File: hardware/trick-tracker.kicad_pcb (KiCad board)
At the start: 4 copper layers, 31 x 45 mm, 53 parts, among them IC1 BMX160, J1 USB4105-GF-A, J2 S2B-PH-K, J3 QWiiC, J4 MEM2061-01-188-00-A, J6 QWiiC, P1 SMTB-1240-S-R, U1 MS88SF2, U2 DPS368XTSA1, U4 MCP73831/OT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

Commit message: Add Gerbers
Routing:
- net GND: vias 41 -> 44

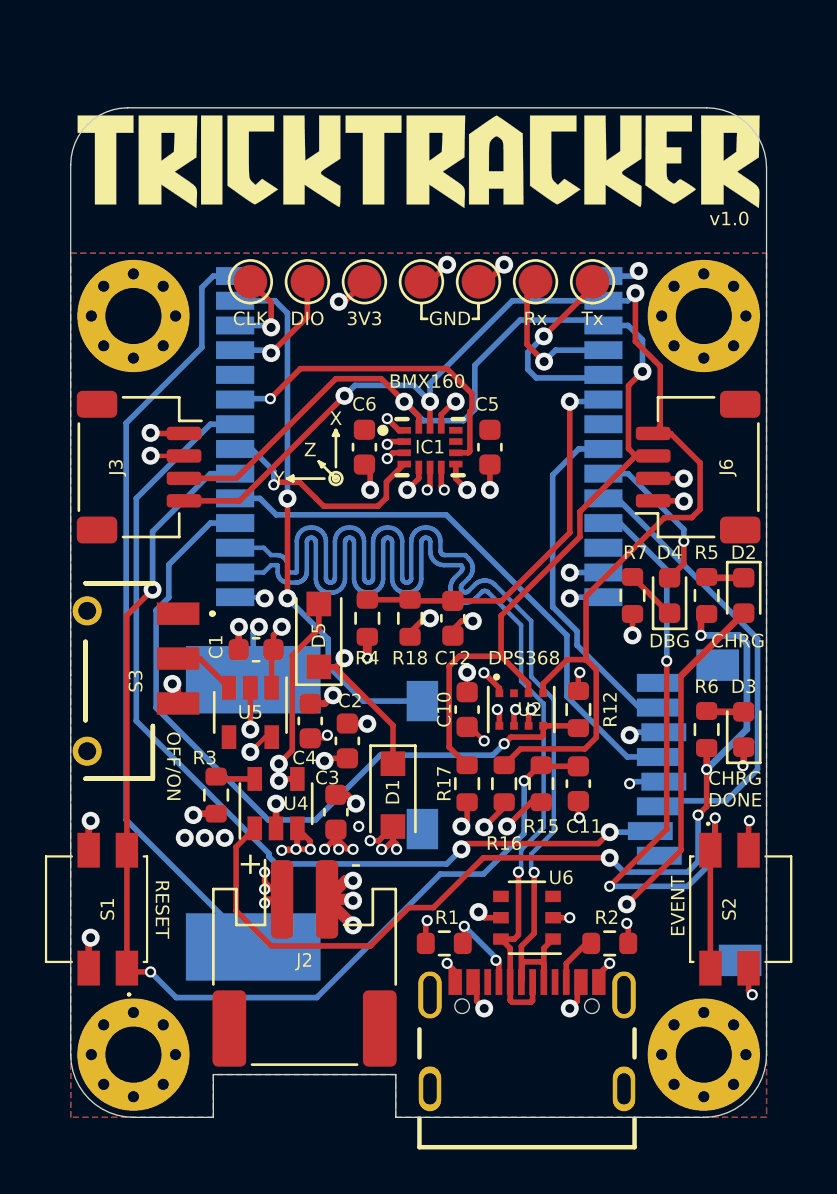
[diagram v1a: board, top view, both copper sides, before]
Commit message: Changed Layout to use ESP32 instead of nRF52
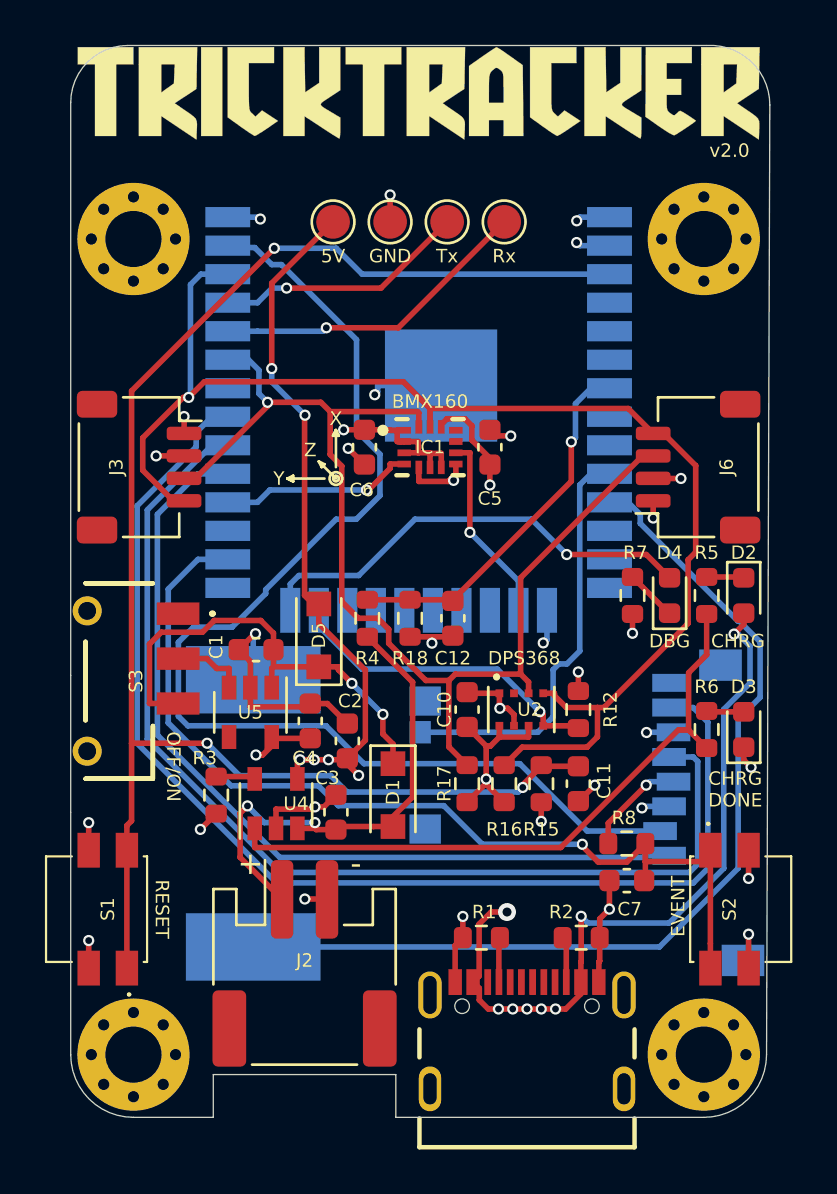
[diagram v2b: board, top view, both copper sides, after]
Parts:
- removed TP5: TP_3v3, TestPoint:TestPoint_Pad_D1.5mm
- removed TP6, TP7: TP_GND, TestPoint:TestPoint_Pad_D1.5mm
- removed U1: MS88SF2, MS88SF2:MS88SF2
- removed U6: IP4220CZ6, Package_SO:TSOP-6_1.65x3.05mm_P0.95mm
- added C7: 0.1µF, Capacitor_SMD:C_0603_1608Metric, F.Cu at (154.8, 126.5)
- added R8: 10k, Resistor_SMD:R_0603_1608Metric, F.Cu at (154.8, 124.8)
- added U3: ESP32-WROOM-32, RF_Module:ESP32-WROOM-32, B.Cu at (145.5, 105.2)
- J4: footprint MEM2061-01-188-00-A_REVA:GCT_MEM2061-01-188-00-A_REVA -> MEM2051-00-195-00-A:GCT_MEM2051-00-195-00-A
- TP1: value TP_Tx -> TestPoint
- TP2: value TP_Rx -> TestPoint
- TP3: value TP_SWDCLK -> TestPoint
- TP4: value TP_SWD -> TestPoint
- moved TP1 11.9 mm to (141.7, 97.2)
- moved TP3 9.16 mm to (146.8, 97.2)
- moved TP4 9.16 mm to (149.4, 97.2)
- moved TP2 7.00 mm to (144.3, 97.2)
- moved H3 3.43 mm to (132.8, 97.9)
- moved H4 3.43 mm to (158.2, 97.9)
- moved G*** 3.05 mm to (145.5, 91.4)
- moved R1 1.67 mm to (148.3, 129.0)
- moved R2 1.30 mm to (152.8, 129.0)
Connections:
- net /3.3V renamed +3V3
- IC1 pad 10: Net-(IC1-Pad10) -> unconnected-(IC1-Pad10)
- IC1 pad 11: Net-(IC1-Pad11) -> unconnected-(IC1-Pad11)
- J1 pad A6: /D+ -> unconnected-(J1-PadA6)
- J1 pad A7: /D- -> unconnected-(J1-PadA7)
- J1 pad A8: Net-(J1-PadA8) -> unconnected-(J1-PadA8)
- J1 pad B6: /D+ -> unconnected-(J1-PadB6)
- J1 pad B7: /D- -> unconnected-(J1-PadB7)
- J1 pad B8: Net-(J1-PadB8) -> unconnected-(J1-PadB8)
- J1 pad S1: Net-(J1-PadS1) -> unconnected-(J1-PadS1)
- J1 pad S2: Net-(J1-PadS2) -> unconnected-(J1-PadS2)
- J1 pad S3: Net-(J1-PadS3) -> unconnected-(J1-PadS3)
- J1 pad S4: Net-(J1-PadS4) -> unconnected-(J1-PadS4)
- J4 pad 1: Net-(J4-Pad1) -> /CS
- J4 pad 2: /CS -> /MOSI
- J4 pad 3: /MOSI -> GND
- J4 pad 5: /SCK -> /CLK
- J4 pad 8: Net-(J4-Pad8) -> unconnected-(J4-Pad8)
- S3 pad 1: Net-(S3-Pad1) -> unconnected-(S3-Pad1)
- S3 pad MH1: Net-(S3-PadMH1) -> unconnected-(S3-PadMH1)
- S3 pad MH2: Net-(S3-PadMH2) -> unconnected-(S3-PadMH2)
- TP1 pad 1: /Tx -> /VBUS
- TP2 pad 1: /Rx -> GND
- TP3 pad 1: /SWDCLK -> /Tx
- TP4 pad 1: /SWDIO -> /Rx
- U2 pad 2: Net-(U2-Pad2) -> unconnected-(U2-Pad2)
- U5 pad 4: Net-(U5-Pad4) -> unconnected-(U5-Pad4)
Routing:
- net /D+: track 54.0 -> 0.00 mm, vias 1 -> 0
- net /D-: track 51.8 -> 0.00 mm, vias 1 -> 0
- net /CLK: track 0.00 -> 48.0 mm
- net /MISO: track 15.6 -> 53.4 mm
- net /VBUS: track 28.8 -> 64.8 mm, vias 7 -> 14
- net /MOSI: track 20.3 -> 53.5 mm
- net /SCK: track 25.3 -> 0.00 mm
- net /RESET: track 51.0 -> 71.6 mm
- net /PRESS_INT: track 33.2 -> 14.4 mm
- net Net-(D4-Pad2): track 7.03 -> 20.3 mm
- net /STAT: track 42.1 -> 29.0 mm, vias 4 -> 0
- net GND: track 49.3 -> 60.4 mm, vias 44 -> 27
- net /BTN: track 32.6 -> 43.2 mm, vias 3 -> 1
- net /VIN: track 11.3 -> 20.8 mm, vias 3 -> 2
- net Net-(P1-Pad1): track 34.8 -> 43.0 mm
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- removed copper zone on B.Cu, net GND
- removed copper zone on F.Cu, net GND
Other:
- board size 31 x 45 mm -> 31.1 x 47.7 mm
- net class Default removed
- board text added: "5V"
- board text added: "v2.0"
- board text removed: "3V3"
- board text removed: "CLK"
- board text removed: "DIO"
- board text removed: "v1.0"
